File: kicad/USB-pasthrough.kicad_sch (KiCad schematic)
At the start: 95 parts, among them J1 USB_Power, J10 SD-1-A, J2 USB_C, J3 Cortex Debug, J4 Power_Sel, J5 SPI Display, J6 SWD, J7 USB_A, J8 MicroSD, J9 Serial, SW1 Boot0, SW2 Reset, U1 AMS1117, U2 STM32F723VET6, Y1 8 MHz

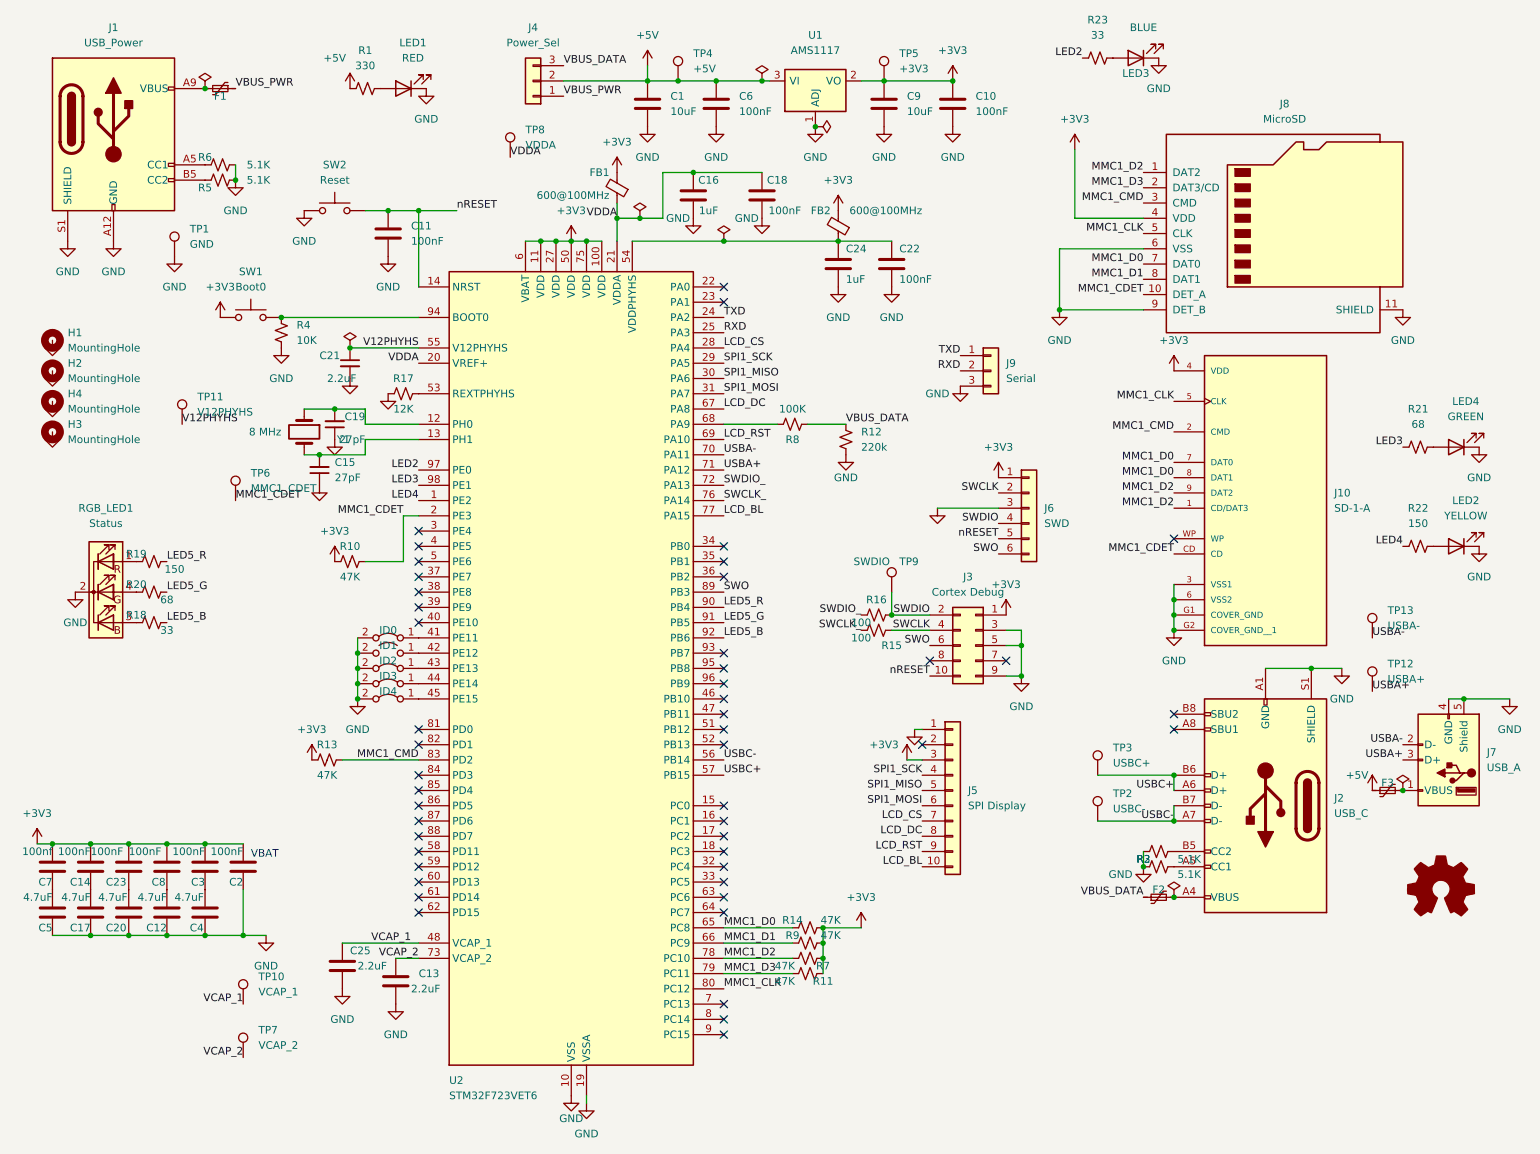
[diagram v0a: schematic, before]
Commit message: Rename MMC1_* signals to SD1_* in schematic and CLAUDE.md
Co-Authored-By: Claude Sonnet 4.6 <noreply@anthropic.com>
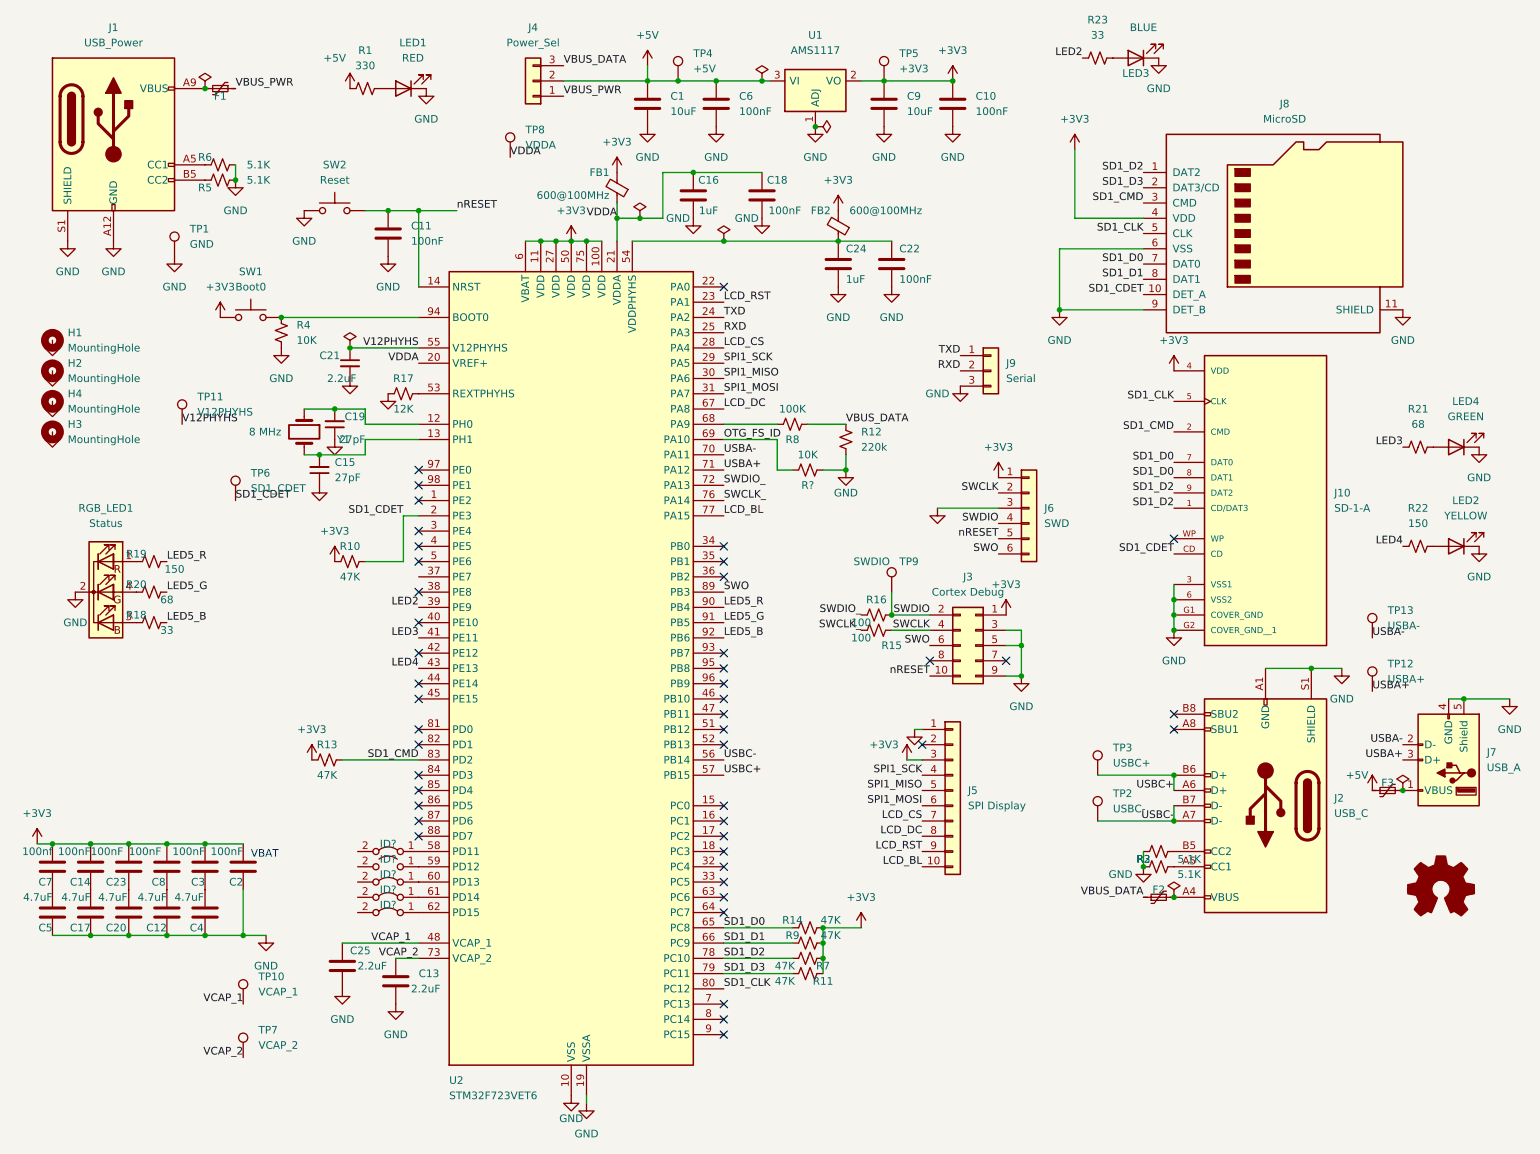
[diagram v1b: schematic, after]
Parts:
- removed ID0, ID2, ID3, ID4: Jumper_2_Bridged, Jumper:SolderJumper-2_P1.3mm_Bridged_Pad1.0x1.5mm, symbol Jumper:Jumper_2_Bridged
- removed ID1: Jumper_2_Bridged, Jumper:SolderJumper-2_P1.3mm_Open_Pad1.0x1.5mm, symbol Jumper:Jumper_2_Open
- added ID? (x4): Jumper_2_Bridged, Jumper:SolderJumper-2_P1.3mm_Bridged_Pad1.0x1.5mm, symbol Jumper:Jumper_2_Bridged
- added ID?: Jumper_2_Bridged, Jumper:SolderJumper-2_P1.3mm_Open_Pad1.0x1.5mm, symbol Jumper:Jumper_2_Open
- added R?: 10K, Resistor_SMD:R_0603_1608Metric_Pad0.98x0.95mm_HandSolder, symbol Device:R_Small_US
- TP6: value MMC1_CDET -> SD1_CDET
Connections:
- net GND: now also R?.1
- net LCD_RST: now also U2.23 (PA1); no longer U2.69 (PA10)
- net LED2: now also U2.39 (PE9); no longer U2.97 (PE0)
- net LED3: now also U2.41 (PE11); no longer U2.98 (PE1)
- net LED4: now also U2.43 (PE13); no longer U2.1 (PE2)
- net at U2.58 (PD11): now also ID?.1 (A)
- net at U2.59 (PD12): now also ID?.1 (A)
- net at U2.60 (PD13): now also ID?.1 (A)
- net at U2.61 (PD14): now also ID?.1 (A)
- net at U2.62 (PD15): now also ID?.1 (A)
- net MMC1_CDET renamed SD1_CDET
- net MMC1_CLK renamed SD1_CLK
- net MMC1_CMD renamed SD1_CMD
- net MMC1_D0 renamed SD1_D0
- net MMC1_D1 renamed SD1_D1
- net MMC1_D2 renamed SD1_D2
- net MMC1_D3 renamed SD1_D3
- new net OTG_FS_ID: R?.2, U2.69 (PA10)
- no-connect marks 48 -> 46
